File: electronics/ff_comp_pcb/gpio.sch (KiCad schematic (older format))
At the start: 38 parts, among them J1 Micro_SD_Card_Det_Hirose_DM3AT, J2 USB_A, U2 A33, U3 FSUSB42MUX, U4 RTL8188CUS, U5 RTL8188CUS, Y1 24Mhz, Y2 32.768khz

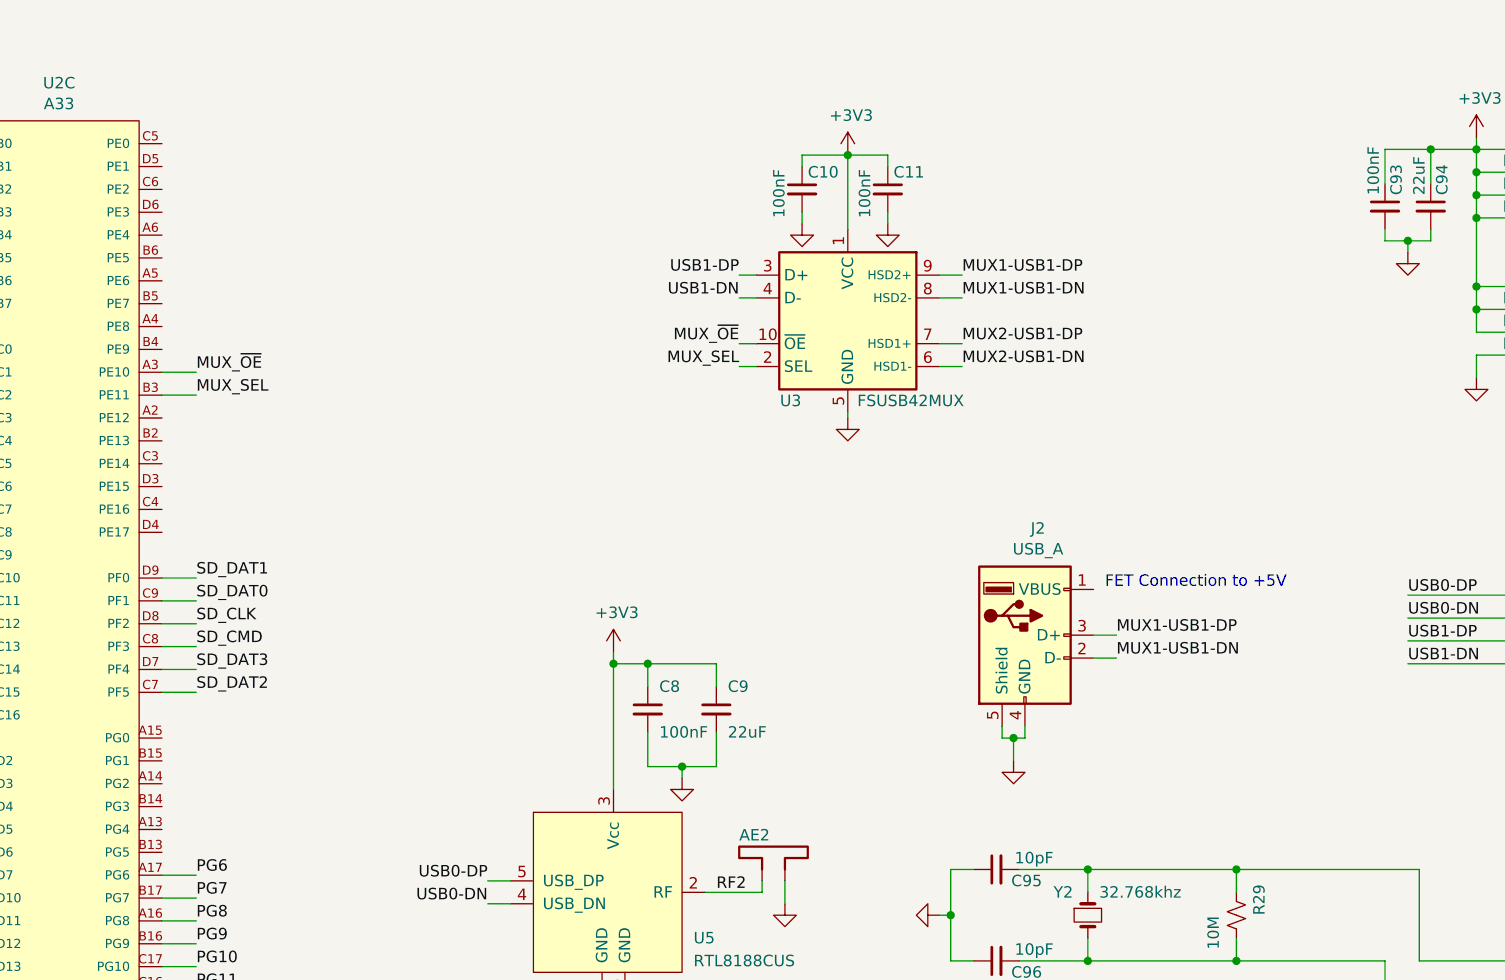
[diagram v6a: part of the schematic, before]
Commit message: Added a fet to switching the 5V.
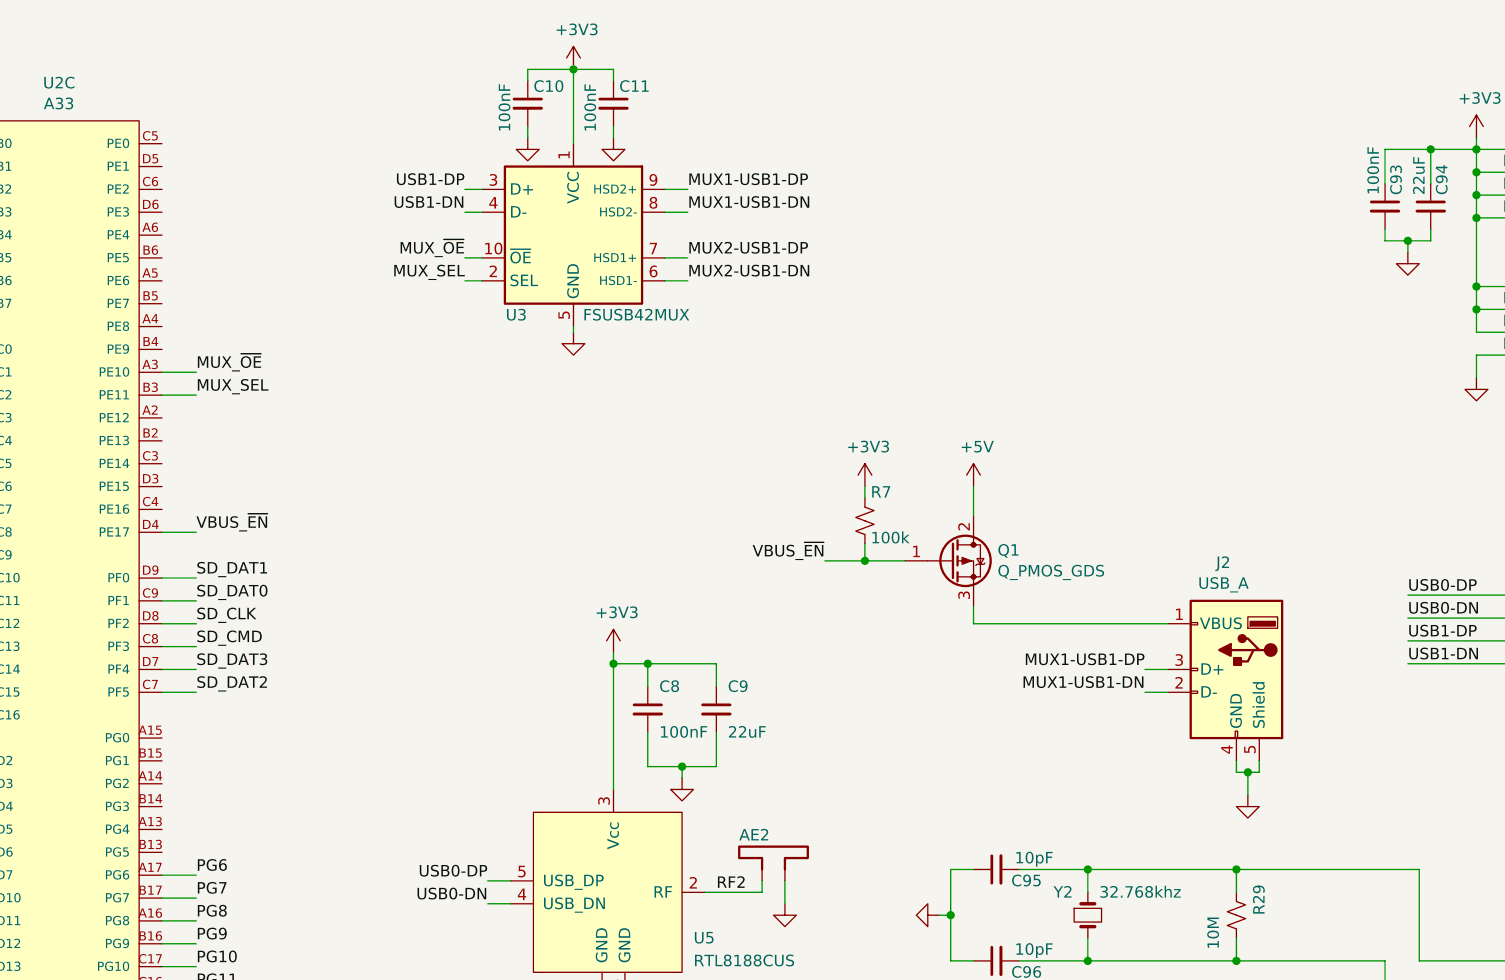
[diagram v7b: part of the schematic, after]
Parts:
- added Q1: Q_PMOS_GDS, symbol Device:Q_PMOS_GDS
- added R7: 100k, Resistor_SMD:R_0402_1005Metric, symbol Device:R_Small_US
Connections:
- net +3V3: now also R7.1
- net VBUS_~EN: now reaches U2.D4 (PE17)
- net VBUS_~EN: now also Q1.1 (G), R7.2
- net at J2.1 (VBUS): now also Q1.3 (S)
- new net +5V: Q1.2 (D)
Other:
- note removed: "FET Connection to +5V"
- moved on the sheet: C10, C11, J2, U3

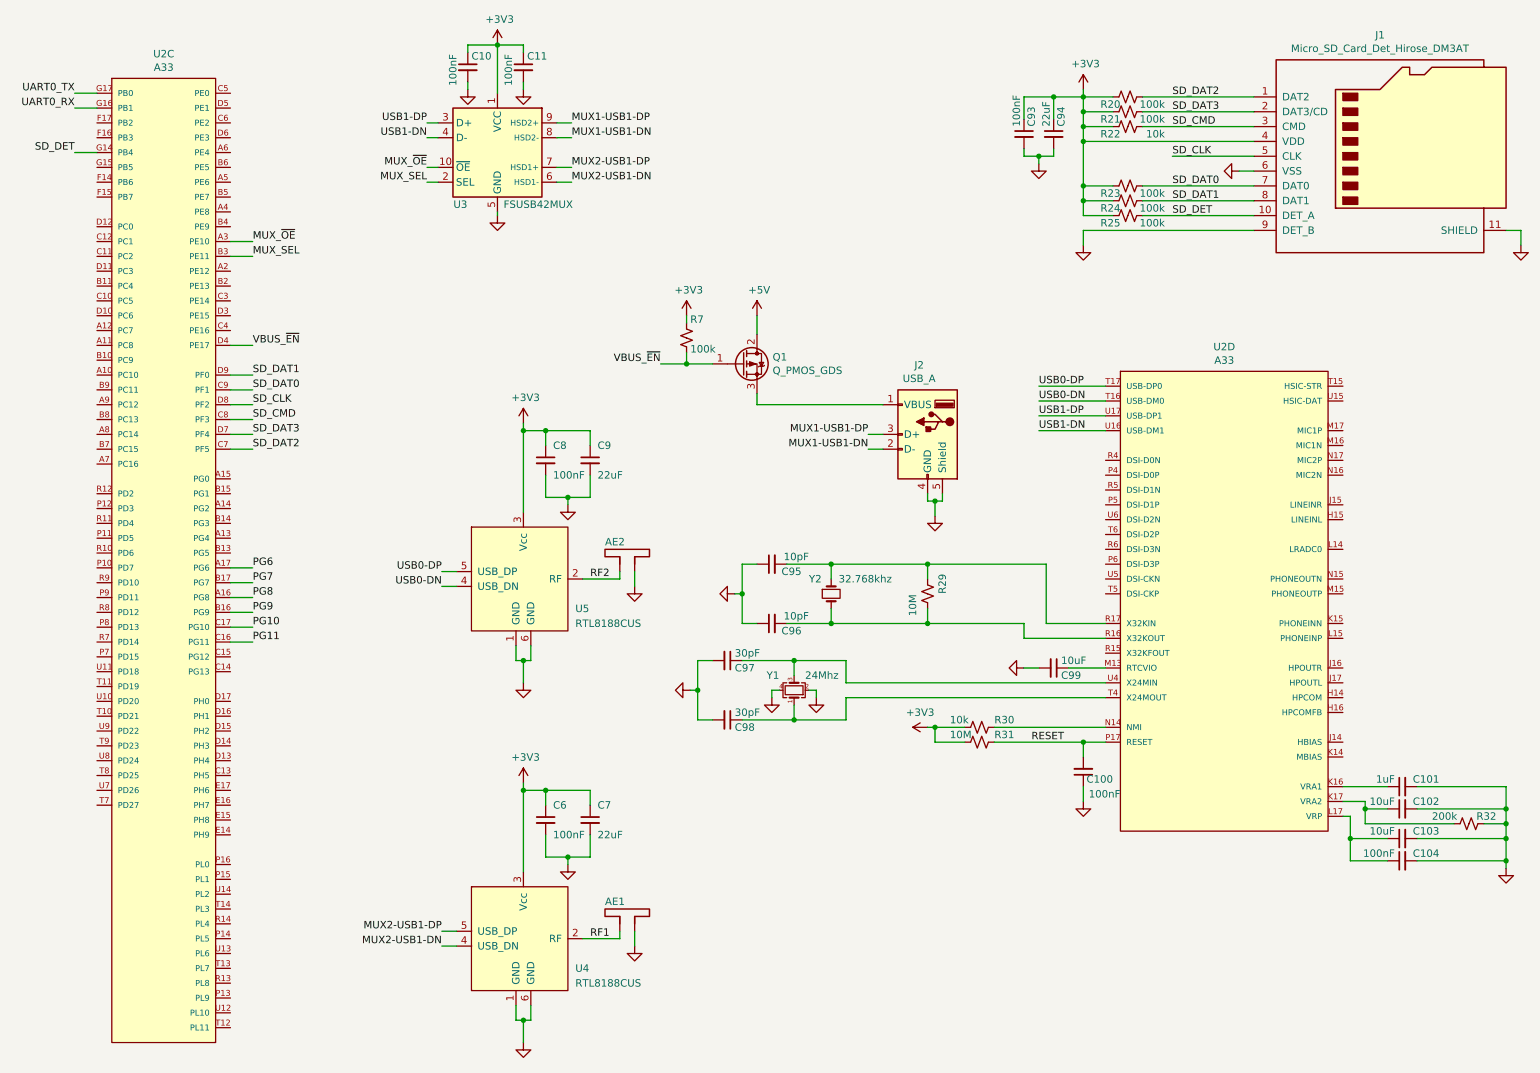
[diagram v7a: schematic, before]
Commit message: Power distrobution IP on the CPU board. Transistors in for 5V control. Part numbers in.
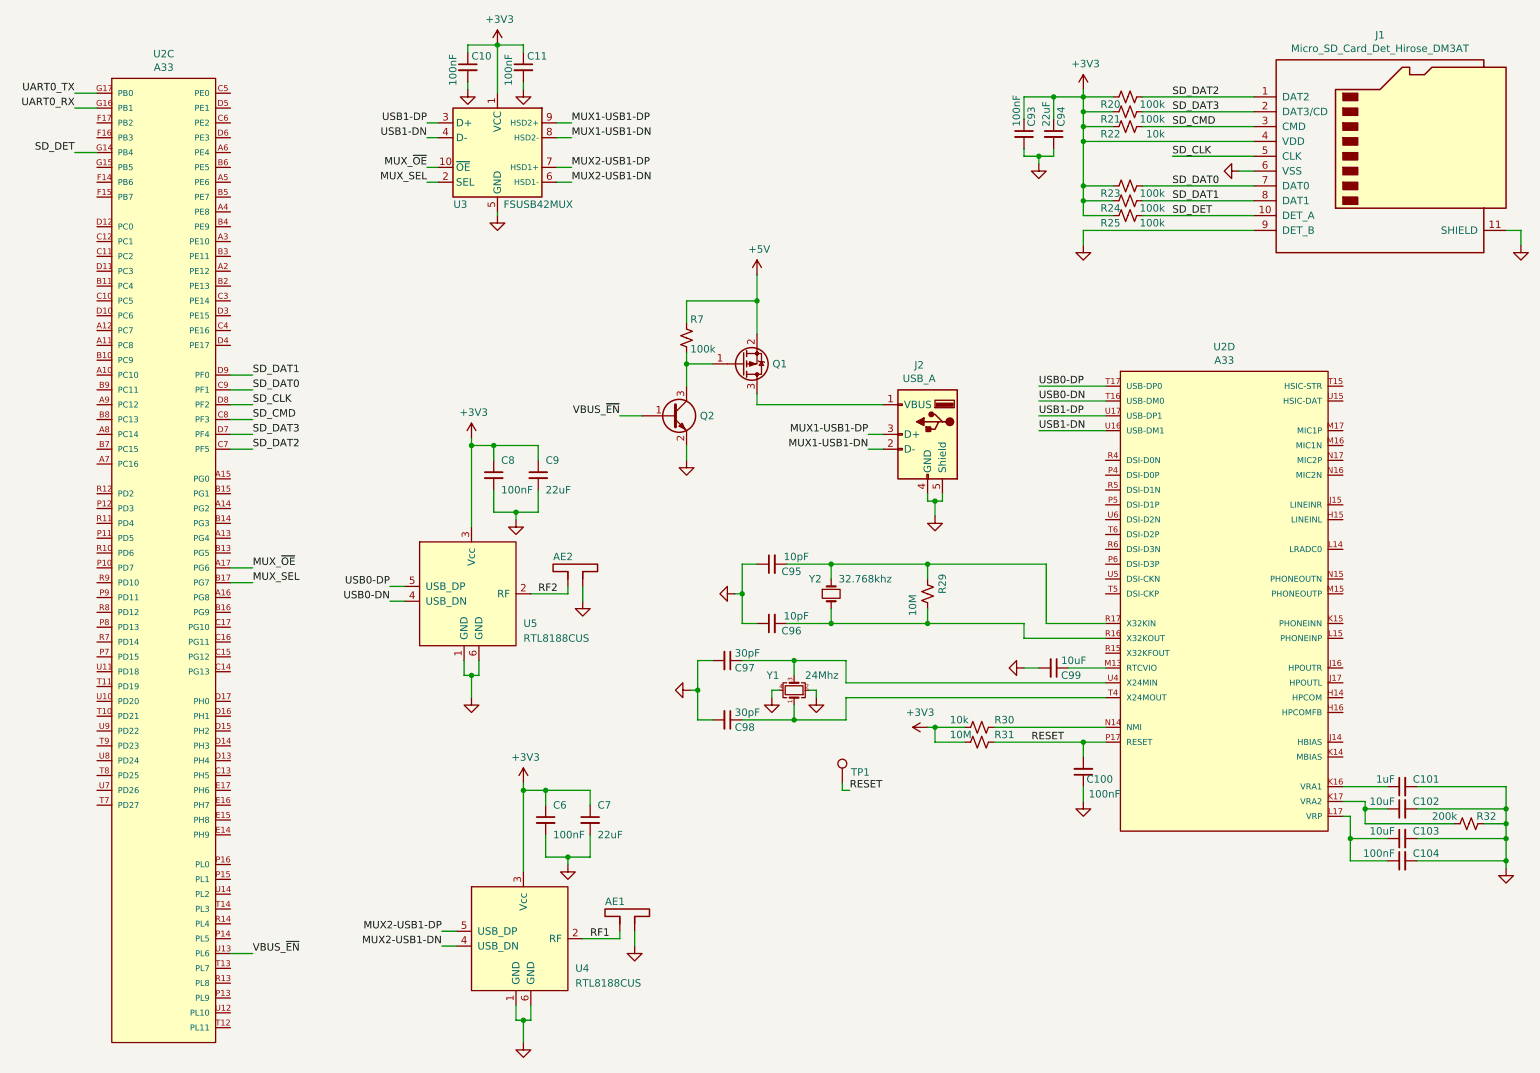
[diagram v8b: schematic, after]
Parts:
- removed Q1: Q_PMOS_GDS, symbol Device:Q_PMOS_GDS
- added Q1: Q_PMOS_GSD, Package_TO_SOT_SMD:SOT-23, symbol Device:Q_PMOS_GSD
- added Q2: Q_NPN_BEC, Package_TO_SOT_SMD:SOT-23, symbol Device:Q_NPN_BEC
- added TP1: TestPoint, TestPoint:TestPoint_Pad_2.0x2.0mm, symbol Connector:TestPoint
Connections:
- net PG6 is gone; now on net MUX_~OE: U2.A17 (PG6)
- net PG7 is gone; now on net MUX_SEL: U2.B17 (PG7)
- net +3V3: no longer R7.1
- net +5V: now also R7.1, Q1.2 (S)
- net GND: now also Q2.2 (E)
- net MUX_SEL: no longer U2.B3 (PE11)
- net MUX_~OE: no longer U2.A3 (PE10)
- net RESET: now also TP1.1
- net VBUS_~EN: now also U2.U13 (PL6), Q2.1 (B); no longer R7.2, U2.D4 (PE17)
- net at J2.1 (VBUS): now also Q1.3 (D)
- net PG10: no longer names the net of U2.C17 (PG10)
- net PG11: no longer names the net of U2.C16 (PG11)
- net PG8: no longer names the net of U2.A16 (PG8)
- net PG9: no longer names the net of U2.B16 (PG9)
- new net: Q1.1 (G), Q2.3 (C), R7.2
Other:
- moved on the sheet: AE2, C8, C9, U5
